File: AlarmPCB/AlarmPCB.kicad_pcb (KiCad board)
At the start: 2 copper layers, 13 parts

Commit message: Made PCB
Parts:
- A1, PB5, PB6, R1, R2: moved to B.Cu
- BZ1: footprint Buzzer_Beeper:Buzzer_12x9.5RM7.6 -> Buzzer_Beeper:Buzzer_D14mm_H7mm_P10mm; moved to B.Cu
- PB1, PB2, PB4, PB7: footprint Button_Switch_THT:Push_E-Switch_KS01Q01 -> Button_Switch_THT:SW_TH_Tactile_Omron_B3F-10xx
- moved RV1 166.5 mm to (75.7, 159.5), turned to 90 degrees
- moved PB4 159.7 mm to (74.2, 134.4)
- moved PB7 157.4 mm to (74.2, 145.5)
- moved PB2 138.6 mm to (74.2, 123.2)
- moved BZ1 127.3 mm to (151.6, 155.7)
- moved PB1 117.6 mm to (74.2, 112.0)
- moved DS1 87.6 mm to (91.4, 119.4)
- moved R2 78.9 mm to (102.4, 130.3)
- moved R1 78.3 mm to (102.6, 140.2)
- moved A1 74.5 mm to (107.7, 159.8)
- moved R3 62.2 mm to (150.9, 111.5)
- moved PB6 58.1 mm to (153.9, 130.3)
- moved PB5 48.2 mm to (153.9, 144.0)
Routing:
- net GND: track 0.00 -> 227.1 mm
- net +5V: track 0.00 -> 150.6 mm, vias 0 -> 1
- net /A4: track 0.00 -> 80.5 mm
- net Net-(A1-Pad9): track 0.00 -> 75.4 mm
- net /A3: track 0.00 -> 74.8 mm
- net Net-(A1-Pad24): track 0.00 -> 60.7 mm
- net /D7: track 0.00 -> 59.2 mm, vias 0 -> 1
- net /D6: track 0.00 -> 56.0 mm
- net Net-(DS1-Pad3): track 0.00 -> 51.6 mm, vias 0 -> 1
- net /A2: track 0.00 -> 37.0 mm, vias 0 -> 1
- net Net-(DS1-Pad16): track 0.00 -> 35.6 mm
- net /A1: track 0.00 -> 29.4 mm
- net /D5: track 0.00 -> 17.0 mm
- net /D4: track 0.00 -> 17.0 mm
- net /D3: track 0.00 -> 17.0 mm
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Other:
- board outline added: 96 x 56.9 mm

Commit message: Fixed Layout Issues
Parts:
- removed PB7: Backlight, Button_Switch_THT:SW_TH_Tactile_Omron_B3F-10xx
- added H1: MountingHole, MountingHole:MountingHole_3.2mm_M3_DIN965_Pad, F.Cu at (139.0, 99.0)
- added H2: MountingHole, MountingHole:MountingHole_3.2mm_M3_DIN965_Pad, F.Cu at (151.0, 160.0)
- added H3: MountingHole, MountingHole:MountingHole_3.2mm_M3_DIN965_Pad, F.Cu at (75.0, 99.0)
- added H4: MountingHole, MountingHole:MountingHole_3.2mm_M3_DIN965_Pad, F.Cu at (75.0, 160.0)
- added PB3: CancelAlarm, Connector_PinHeader_2.54mm:PinHeader_1x02_P2.54mm_Vertical, B.Cu at (133.3, 161.8)
- DS1: footprint Display:WC1602A -> ECE:WC1602A
- PB1: value Time+ -> Backlight; footprint Button_Switch_THT:SW_TH_Tactile_Omron_B3F-10xx -> ECE:SW_TH_Tactile
- PB2: value Time- -> Snooze; footprint Button_Switch_THT:SW_TH_Tactile_Omron_B3F-10xx -> Connector_PinHeader_2.54mm:PinHeader_1x02_P2.54mm_Vertical; moved to B.Cu
- PB4: footprint Button_Switch_THT:SW_TH_Tactile_Omron_B3F-10xx -> ECE:SW_TH_Tactile
- PB5: value CancelAlarm -> Time-; footprint Button_Switch_THT:Push_E-Switch_KS01Q01 -> ECE:SW_TH_Tactile; moved to F.Cu
- PB6: value Snooze -> Time+; footprint Button_Switch_THT:Push_E-Switch_KS01Q01 -> ECE:SW_TH_Tactile; moved to F.Cu
- R1: value 220R -> PhotoResistor; footprint Resistor_THT:R_Axial_DIN0309_L9.0mm_D3.2mm_P12.70mm_Horizontal -> Connector_PinHeader_2.54mm:PinHeader_1x02_P2.54mm_Vertical; moved to F.Cu
- R3: value PhotoResistor -> 220R; footprint OptoDevice:R_LDR_4.9x4.2mm_P2.54mm_Vertical -> Resistor_THT:R_Axial_DIN0309_L9.0mm_D3.2mm_P12.70mm_Horizontal; moved to B.Cu
- RV1: footprint Potentiometer_THT:Potentiometer_ACP_CA6-H2,5_Horizontal -> digikey-footprints:Potentiometer_P120PK-Y25BR10K
- moved PB1 95.2 mm to (158.4, 156.4)
- moved PB4 85.0 mm to (158.4, 145.4)
- moved PB2 76.1 mm to (139.7, 161.8), turned to 270 degrees
- moved BZ1 52.0 mm to (157.0, 104.0), turned to 270 degrees
- moved R3 32.7 mm to (120.4, 99.6), turned to 180 degrees
- moved R2 31.1 mm to (104.1, 161.3)
- moved R1 30.9 mm to (125.0, 161.5), turned to 270 degrees
- moved RV1 24.2 mm to (97.5, 149.0), turned to 180 degrees
- moved DS1 11.9 mm to (82.3, 111.8)
- moved PB5 10.6 mm to (158.4, 134.4)
- moved PB6 8.23 mm to (158.4, 123.4)
- moved A1 4.63 mm to (105.0, 156.0)
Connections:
- PB1 pad 1: /D6 -> /A3
- PB2 pad 1: /D7 -> /A2
- PB5 pad 1: /A1 -> /D7
- PB6 pad 1: /A2 -> /D6
- R1 pad 1: Net-(DS1-Pad16) -> Net-(A1-Pad9)
- R1 pad 2: GND -> +5V
- R3 pad 1: Net-(A1-Pad9) -> Net-(DS1-Pad16)
- R3 pad 2: +5V -> GND
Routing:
- net GND: track 227.1 -> 0.00 mm
- net +5V: track 150.6 -> 45.6 mm, vias 1 -> 0
- net Net-(A1-Pad9): track 75.4 -> 17.6 mm
- net /A4: track 80.5 -> 31.3 mm
- net /A3: track 74.8 -> 30.3 mm
- net Net-(DS1-Pad3): track 51.6 -> 8.96 mm, vias 1 -> 0
- net /A2: track 37.0 -> 9.16 mm, vias 1 -> 0
- net Net-(DS1-Pad16): track 35.6 -> 12.2 mm
- net /A1: track 29.4 -> 7.02 mm
- net Net-(A1-Pad24): track 60.7 -> 42.4 mm
- net /D6: track 56.0 -> 46.7 mm
- net /D10: track 13.9 -> 6.12 mm
- net /D2: track 17.0 -> 24.2 mm
- net /D7: track 59.2 -> 53.2 mm, vias 1 -> 0
- net /D12: track 15.5 -> 20.5 mm, vias 1 -> 0
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- added copper zone on B.Cu, net GND
- added copper zone on F.Cu, net GND
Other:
- board size 96 x 56.9 mm -> 100 x 71 mm
- rule trace_min: 0.254 -> 0.1
- rule via_min_size: 1.016 -> 0.2

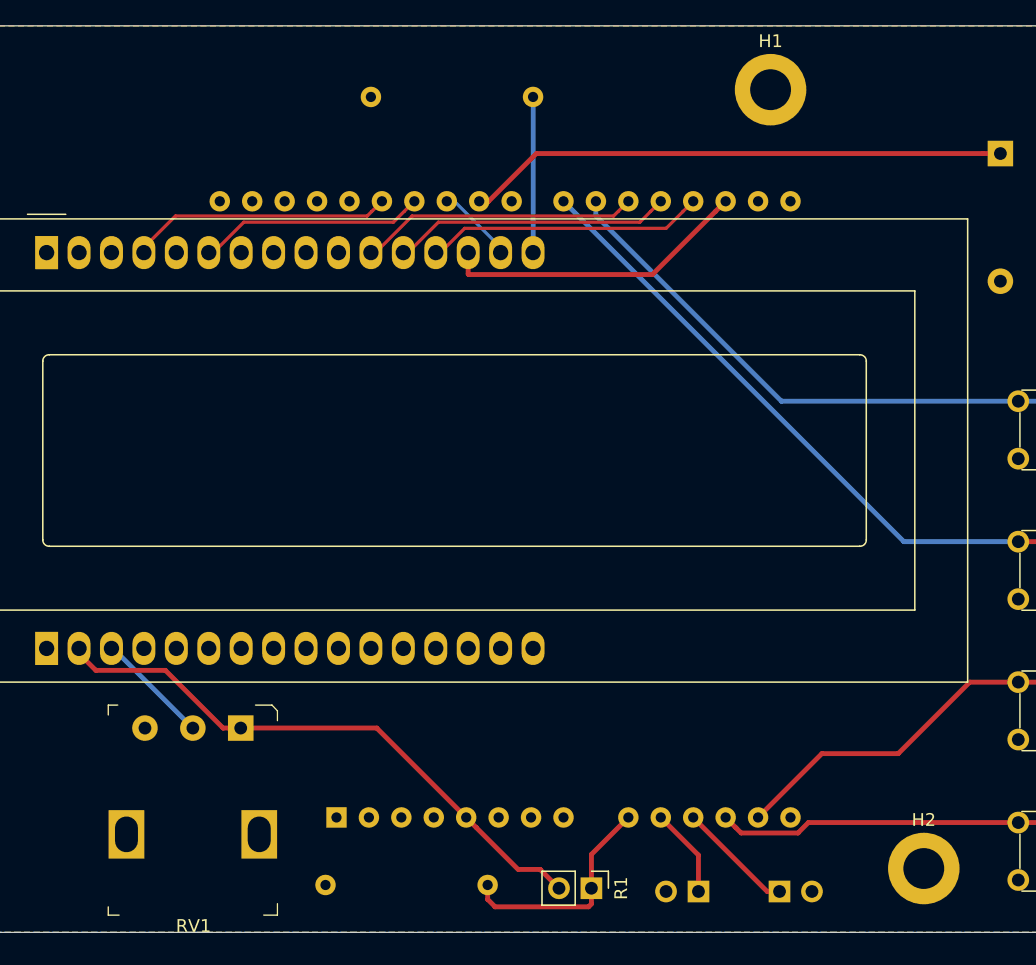
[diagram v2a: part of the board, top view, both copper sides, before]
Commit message: Moved pot
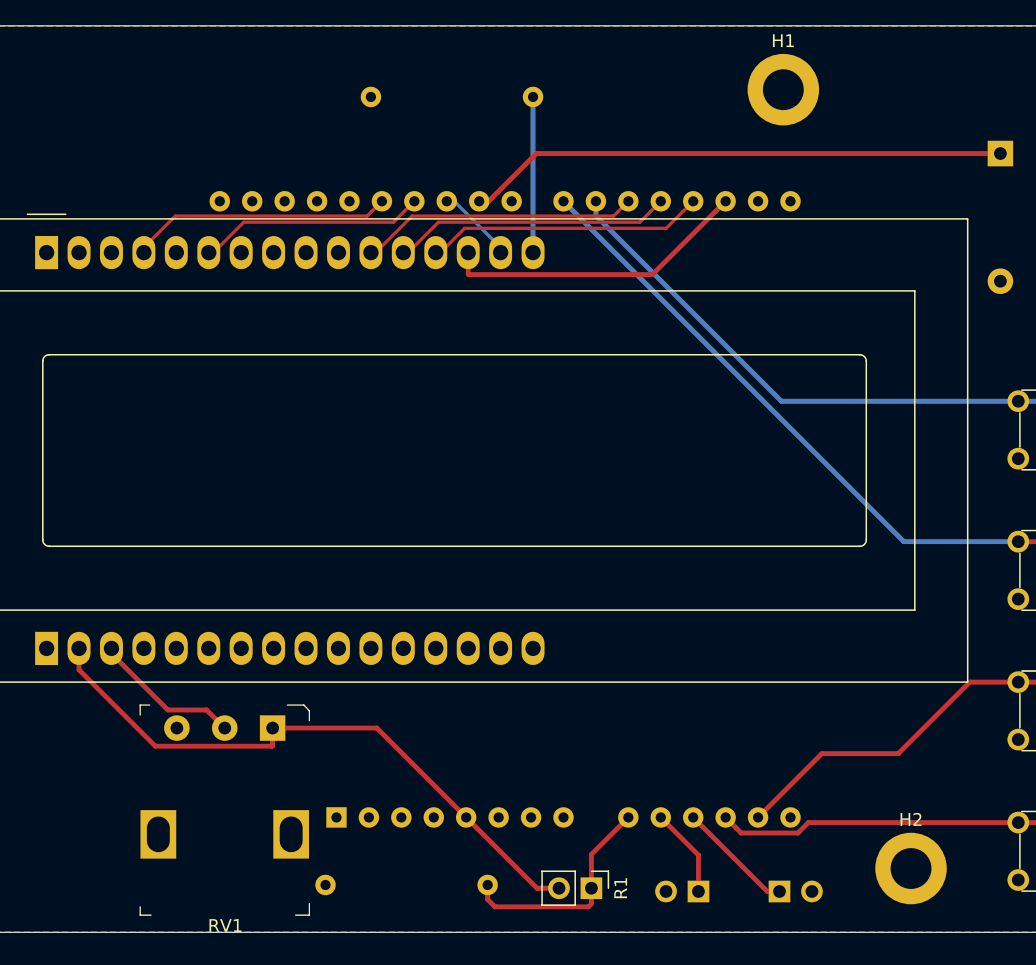
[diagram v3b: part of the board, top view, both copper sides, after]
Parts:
- moved RV1 2.50 mm to (100.0, 149.0)
- moved H1 1.00 mm to (140.0, 99.0)
- moved H2 1.00 mm to (150.0, 160.0)
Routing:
- net Net-(DS1-Pad3): track 8.96 -> 11.8 mm
- net +5V: track 45.6 -> 48.3 mm

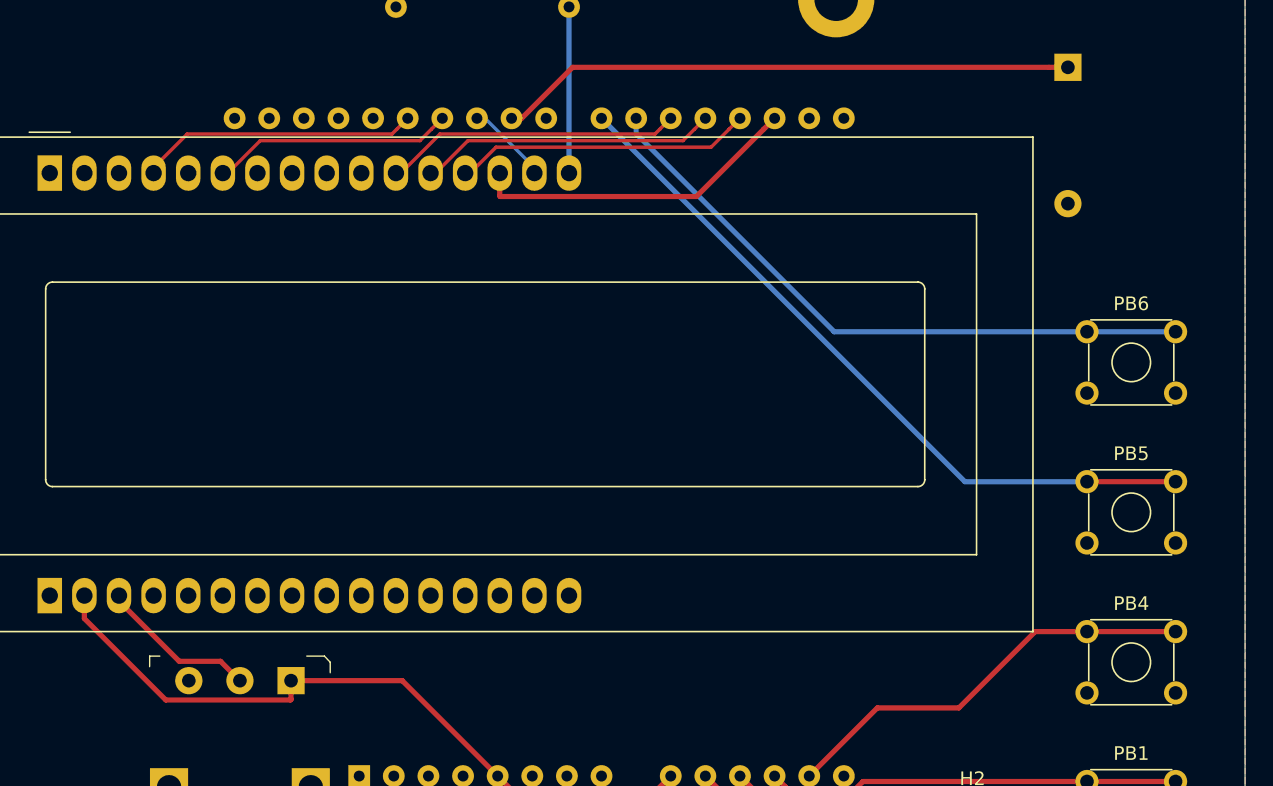
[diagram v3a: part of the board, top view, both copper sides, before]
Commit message: Added more hole to track clerance
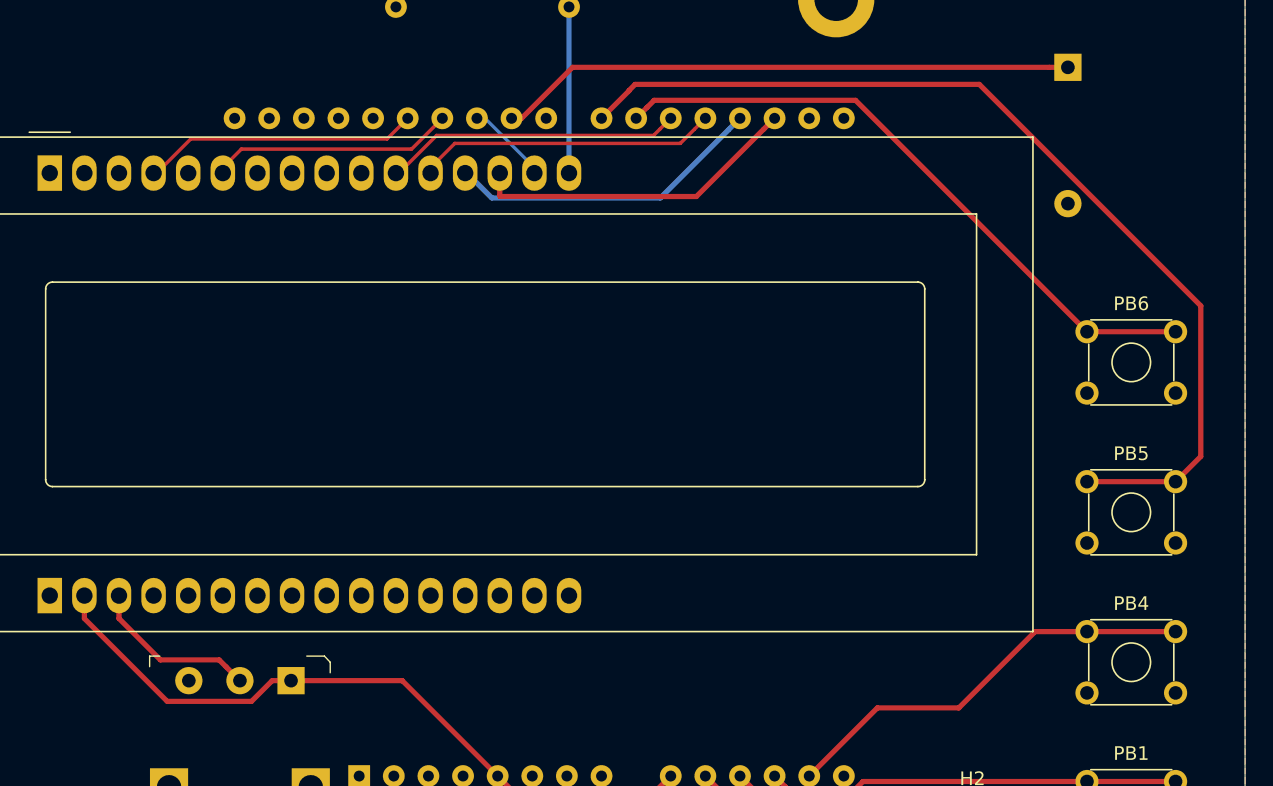
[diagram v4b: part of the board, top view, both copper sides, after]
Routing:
- net /D7: track 53.2 -> 71.9 mm
- net /D3: track 21.8 -> 23.3 mm
- net +5V: track 48.3 -> 47.6 mm
- net Net-(DS1-Pad3): track 11.8 -> 12.4 mm
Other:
- net class Default: clearance 0.2286 -> 0.33
- rule trace_clearance: 0.2286 -> 0.33

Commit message: Minor adjustments
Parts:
- moved H1 4.00 mm to (140.0, 95.0)
- moved H3 4.00 mm to (75.0, 95.0)
- moved R2 1.13 mm to (105.2, 161.5)
- moved RV1 0.25 mm to (99.8, 149.0)
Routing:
- net +5V: track 47.6 -> 45.6 mm
- net Net-(A1-Pad9): track 17.6 -> 16.3 mm
- net Net-(DS1-Pad3): track 12.4 -> 11.4 mm
- net /A3: track 30.3 -> 30.9 mm
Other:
- board size 100 x 71 mm -> 100 x 75 mm
